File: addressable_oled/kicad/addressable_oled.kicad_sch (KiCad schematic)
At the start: 1 part

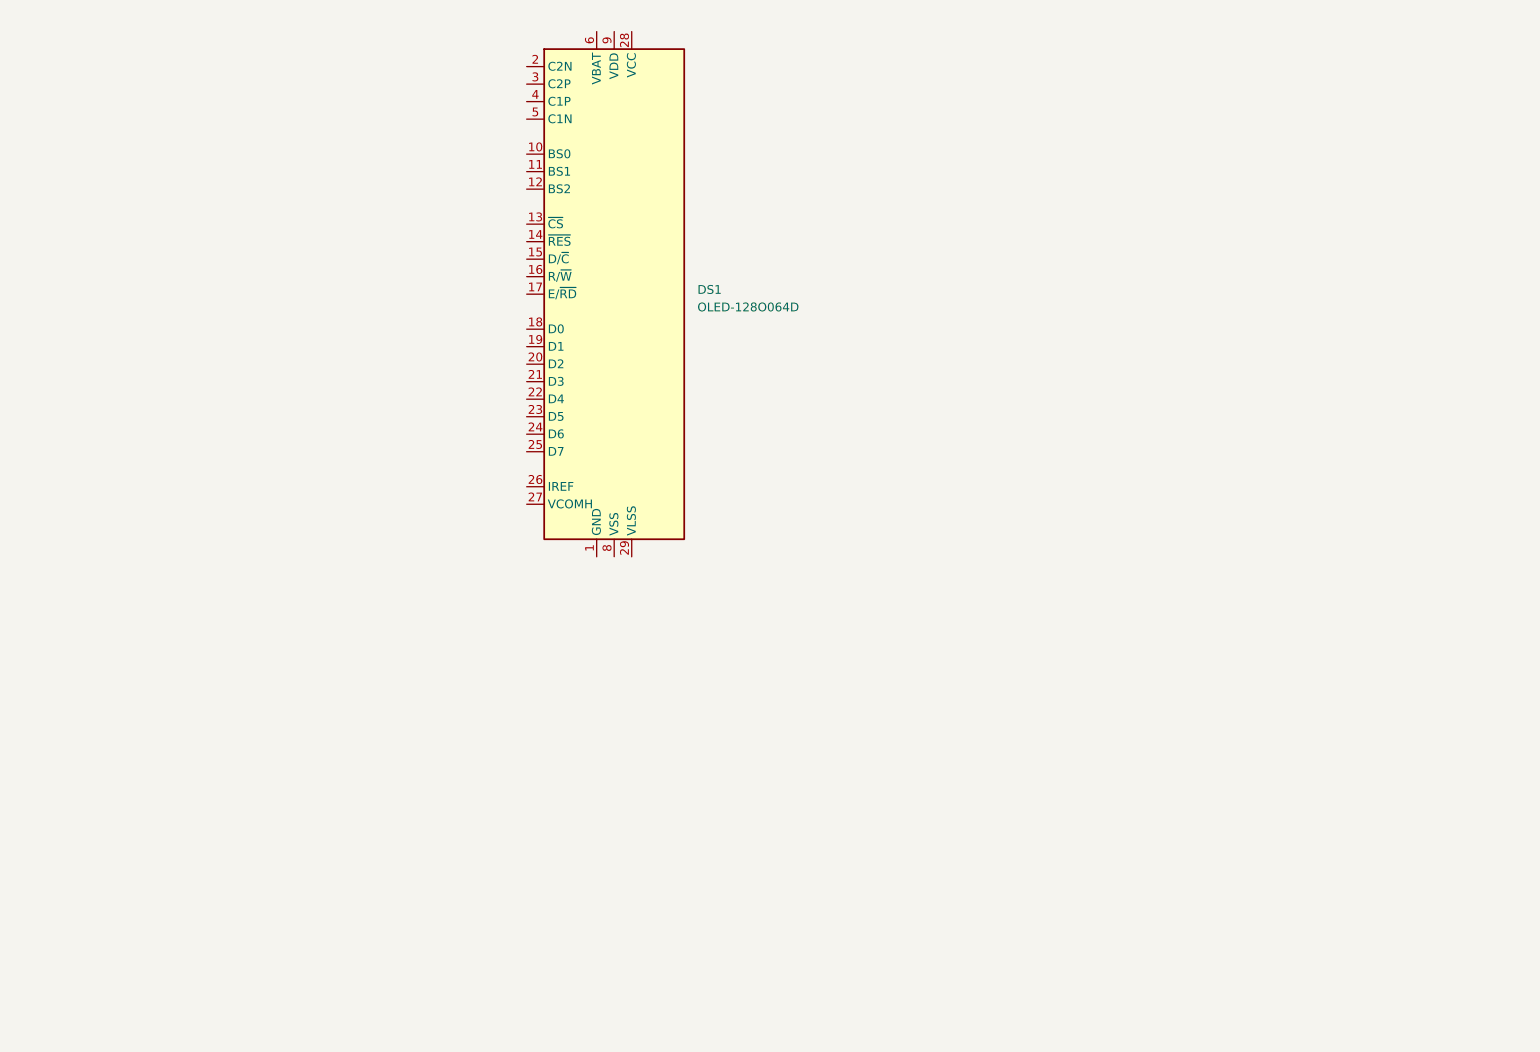
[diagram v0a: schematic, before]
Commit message: Work in progress. Added symbols and footprints.
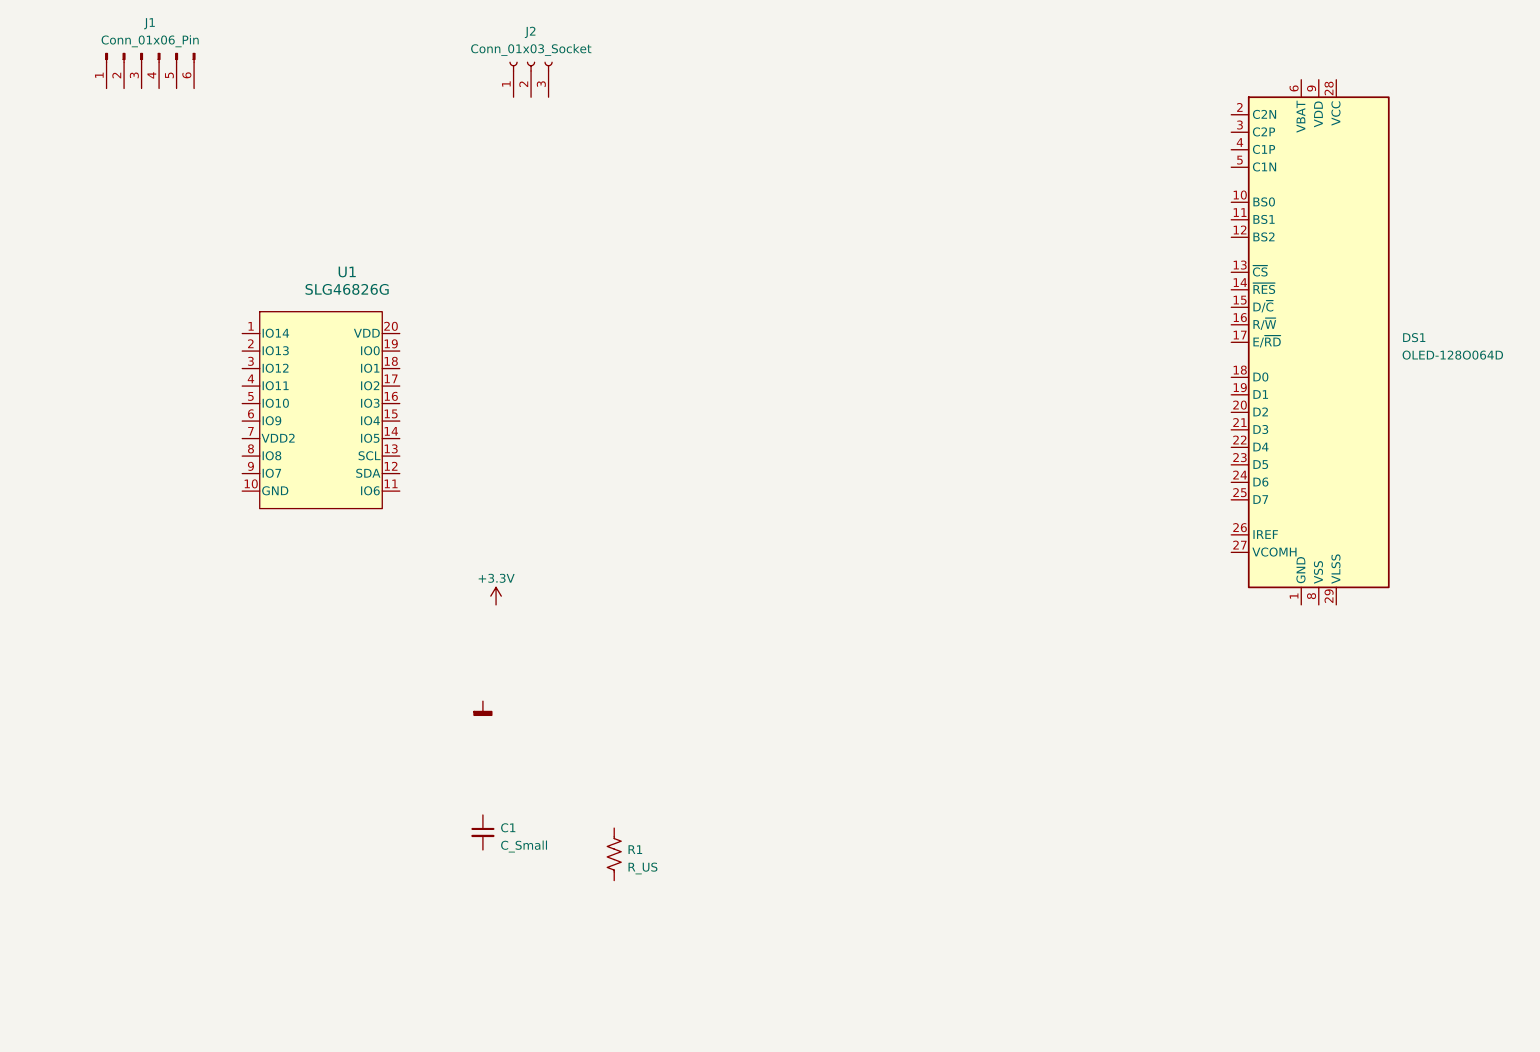
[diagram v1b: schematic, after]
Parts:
- added C1: C_Small, symbol Device:C_Small
- added J1: Conn_01x06_Pin, symbol Connector:Conn_01x06_Pin
- added J2: Conn_01x03_Socket, symbol Connector:Conn_01x03_Socket
- added R1: R_US, symbol Device:R_US
- added U1: SLG46826G, addressable_oled:TSSOP20_MO-220_WECE_REN, symbol addressable_oled:SLG46826G
- DS1: footprint Display:OLED-128O064D -> addressable_oled:OLED-128O064D; symbol Display_Graphic:OLED-128O064D -> addressable_oled:OLED-128O064D
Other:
- moved on the sheet: DS1
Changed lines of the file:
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@@
 (kicad_sch (version 20230121) (generator eeschema)
   (paper "A4")
-  (symbol (lib_id "Display_Graphic:OLED-128O064D") (at 123.825 85.09 0) (unit 1)
-    (in_bom yes) (on_board yes) (dnp no) (fields_autoplaced)
-    (property "Reference" "DS1" (at 135.89 84.455 0)
-      (effects (font (size 1.27 1.27)) (justify left))
-    )
-    (property "Value" "OLED-128O064D" (at 135.89 86.995 0)
-      (effects (font (size 1.27 1.27)) (justify left))
-    )
-    (property "Footprint" "Display:OLED-128O064D" (at 123.825 85.09 0)
-      (effects (font (size 1.27 1.27)) hide)
-    )
-    (property "Datasheet" "https://www.vishay.com/docs/37902/oled128o064dbpp3n00000.pdf" (at 123.825 64.77 0)
+  (symbol (lib_id "Connector:Conn_01x06_Pin") (at 55.245 50.165 90) (mirror x) (unit 1)
+    (in_bom yes) (on_board yes) (dnp no)
+    (property "Reference" "J1" (at 56.515 45.72 90)
+      (effects (font (size 1.27 1.27)))
+    )
+    (property "Value" "Conn_01x06_Pin" (at 56.515 48.26 90)
+      (effects (font (size 1.27 1.27)))
+    )
+    (property "Footprint" "" (at 55.245 50.165 0)
+      (effects (font (size 1.27 1.27)) hide)
+    )
+    (property "Datasheet" "~" (at 55.245 50.165 0)
+      (effects (font (size 1.27 1.27)) hide)
+    )
+    (pin "1")
+    (pin "2")
+    (pin "3")
+    (pin "4")
+    (pin "5")
+    (pin "6")
+    (instances
+      (project "addressable_oled"
+        (path "/7b608d4d-4c17-4227-91f9-c343a36b0392"
+          (reference "J1") (unit 1)
+        )
+      )
+    )
+  )
+  (symbol (lib_id "Device:C_Small") (at 104.775 163.195 0) (unit 1)
+    (in_bom yes) (on_board yes) (dnp no) (fields_autoplaced)
+    (property "Reference" "C1" (at 107.315 162.5663 0)
+      (effects (font (size 1.27 1.27)) (justify left))
+    )
+    (property "Value" "C_Small" (at 107.315 165.1063 0)
+      (effects (font (size 1.27 1.27)) (justify left))
+    )
+    (property "Footprint" "" (at 104.775 163.195 0)
+      (effects (font (size 1.27 1.27)) hide)
+    )
+    (property "Datasheet" "~" (at 104.775 163.195 0)
+      (effects (font (size 1.27 1.27)) hide)
+    )
+    (pin "1")
+    (pin "2")
+    (instances
+      (project "addressable_oled"
+        (path "/7b608d4d-4c17-4227-91f9-c343a36b0392"
+          (reference "C1") (unit 1)
+        )
+      )
+    )
+  )
+  (symbol (lib_id "Device:R_US") (at 123.825 166.37 0) (unit 1)
+    (in_bom yes) (on_board yes) (dnp no) (fields_autoplaced)
+    (property "Reference" "R1" (at 125.73 165.735 0)
+      (effects (font (size 1.27 1.27)) (justify left))
+    )
+    (property "Value" "R_US" (at 125.73 168.275 0)
+      (effects (font (size 1.27 1.27)) (justify left))
+    )
+    (property "Footprint" "" (at 124.841 166.624 90)
+      (effects (font (size 1.27 1.27)) hide)
+    )
+    (property "Datasheet" "~" (at 123.825 166.37 0)
+      (effects (font (size 1.27 1.27)) hide)
+    )
+    (pin "1")
+    (pin "2")
+    (instances
+      (project "addressable_oled"
+        (path "/7b608d4d-4c17-4227-91f9-c343a36b0392"
+          (reference "R1") (unit 1)
+        )
+      )
+    )
+  )
+  (symbol (lib_id "addressable_oled:OLED-128O064D") (at 226.06 92.075 0) (unit 1)
+    (in_bom yes) (on_board yes) (dnp no) (fields_autoplaced)
+    (property "Reference" "DS1" (at 238.125 91.44 0)
+      (effects (font (size 1.27 1.27)) (justify left))
+    )
+    (property "Value" "OLED-128O064D" (at 238.125 93.98 0)
+      (effects (font (size 1.27 1.27)) (justify left))
+    )
+    (property "Footprint" "addressable_oled:OLED-128O064D" (at 226.06 92.075 0)
+      (effects (font (size 1.27 1.27)) hide)
+    )
+    (property "Datasheet" "https://www.vishay.com/docs/37902/oled128o064dbpp3n00000.pdf" (at 226.06 71.755 0)
       (effects (font (size 1.27 1.27)) hide)
     )
@@
         )
       )
+    )
+  )
+  (symbol (lib_id "addressable_oled:GND") (at 104.775 144.145 0) (unit 1)
+    (in_bom yes) (on_board yes) (dnp no) (fields_autoplaced)
+    (property "Reference" "#PWR02" (at 104.775 150.495 0)
+      (effects (font (size 1.27 1.27)) hide)
+    )
+    (property "Value" "GND" (at 104.775 149.225 0)
+      (effects (font (size 1.27 1.27)) hide)
+    )
+    (property "Footprint" "" (at 104.775 144.145 0)
+      (effects (font (size 1.27 1.27)) hide)
+    )
+    (property "Datasheet" "" (at 104.775 144.145 0)
+      (effects (font (size 1.27 1.27)) hide)
+    )
+    (pin "1")
+    (instances
+      (project "addressable_oled"
+        (path "/7b608d4d-4c17-4227-91f9-c343a36b0392"
+          (reference "#PWR02") (unit 1)
+        )
+      )
+    )
+  )
+  (symbol (lib_id "Connector:Conn_01x03_Socket") (at 111.76 51.435 90) (unit 1)
+    (in_bom yes) (on_board yes) (dnp no) (fields_autoplaced)
+    (property "Reference" "J2" (at 111.76 46.99 90)
+      (effects (font (size 1.27 1.27)))
+    )
+    (property "Value" "Conn_01x03_Socket" (at 111.76 49.53 90)
+      (effects (font (size 1.27 1.27)))
+    )
+    (property "Footprint" "" (at 111.76 51.435 0)
+      (effects (font (size 1.27 1.27)) hide)
+    )
+    (property "Datasheet" "~" (at 111.76 51.435 0)
+      (effects (font (size 1.27 1.27)) hide)
+    )
+    (pin "1")
+    (pin "2")
+    (pin "3")
+    (instances
+      (project "addressable_oled"
+        (path "/7b608d4d-4c17-4227-91f9-c343a36b0392"
+          (reference "J2") (unit 1)
+        )
+      )
+    )
+  )
+  (symbol (lib_id "addressable_oled:SLG46826G") (at 64.77 90.805 0) (unit 1)
+    (in_bom yes) (on_board yes) (dnp no) (fields_autoplaced)
+    (property "Reference" "U1" (at 85.09 81.915 0)
+      (effects (font (size 1.524 1.524)))
+    )
+    (property "Value" "SLG46826G" (at 85.09 84.455 0)
+      (effects (font (size 1.524 1.524)))
+    )
+    (property "Footprint" "addressable_oled:TSSOP20_MO-220_WECE_REN" (at 64.77 90.805 0)
+      (effects (font (size 1.27 1.27) italic) hide)
+    )
+    (property "Datasheet" "SLG46826G" (at 64.77 90.805 0)
+      (effects (font (size 1.27 1.27) italic) hide)
+    )
+    (pin "1")
+    (pin "10")
+    (pin "11")
+    (pin "12")
+    (pin "13")
+    (pin "14")
+    (pin "15")
+    (pin "16")
+    (pin "17")
+    (pin "18")
+    (pin "19")
+    (pin "2")
+    (pin "20")
+    (pin "3")
+    (pin "4")
+    (pin "5")
+    (pin "6")
+    (pin "7")
+    (pin "8")
+    (pin "9")
+    (instances
+      (project "addressable_oled"
+        (path "/7b608d4d-4c17-4227-91f9-c343a36b0392"
+          (reference "U1") (unit 1)
+        )
+      )
+    )
+  )
+  (symbol (lib_id "power:+3.3V") (at 106.68 130.175 0) (unit 1)
+    (in_bom yes) (on_board yes) (dnp no) (fields_autoplaced)
+    (property "Reference" "#PWR01" (at 106.68 133.985 0)
+      (effects (font (size 1.27 1.27)) hide)
+    )
+    (property "Value" "+3.3V" (at 106.68 126.365 0)
+      (effects (font (size 1.27 1.27)))
+    )
+    (property "Footprint" "" (at 106.68 130.175 0)
+      (effects (font (size 1.27 1.27)) hide)
+    )
+    (property "Datasheet" "" (at 106.68 130.175 0)
+      (effects (font (size 1.27 1.27)) hide)
+    )
+    (pin "1")
+    (instances
+      (project "addressable_oled"
+        (path "/7b608d4d-4c17-4227-91f9-c343a36b0392"
+          (reference "#PWR01") (unit 1)
+        )
+      )

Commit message: Work in progress. First pass of the schematic.
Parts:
- added C2, C3, C4, C5, C6, C7, C8: C_Small, symbol Device:C_Small
- added JP1, JP2, JP?: Jumper_2_Open, symbol addressable_oled:Jumper_2_Open
- added R5, R6: R_US, symbol Device:R_US
- J1: value Conn_01x06_Pin -> Conn_01x05_Pin; symbol Connector:Conn_01x06_Pin -> Connector:Conn_01x05_Pin
- renumbered DS1 to DS?
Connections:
- net GND: now also C1.1, DS?.1 (GND), DS?.10 (BS0), DS?.11 (BS1), DS?.12 (BS2), DS?.16 (R/~{W}), DS?.17 (E/~{RD}), DS?.20 (D2), DS?.21 (D3), DS?.22 (D4), DS?.23 (D5), DS?.24 (D6), DS?.25 (D7), DS?.29 (VLSS), DS?.30 (GND), DS?.8 (VSS), J1.1 (Pin_1), J2.1 (Pin_1), R1.2, U1.10 (GND), C2.2, C3.1, C4.1, C5.2, C8.1
- net 3V3: now reaches J1.2 (Pin_2)
- net 3V3: now also C1.2, DS?.6 (VBAT), DS?.9 (VDD), U1.20 (VDD), U1.7 (VDD2), C2.1, C3.2, C4.2, JP1.2, JP2.2, JP?.2, R5.1, R6.1
- net CS: now reaches J1.3 (Pin_3)
- net CS: now also U1.1 (IO14)
- net CLK: now reaches J1.4 (Pin_4)
- net CLK: now also U1.2 (IO13)
- net MOSI: now reaches J1.5 (Pin_5)
- net MOSI: now also U1.3 (IO12)
- net at R1.1: now also DS?.26 (IREF)
- net OLED_CS: now reaches DS?.13 (~{CS})
- net OLED_CS: now also U1.4 (IO11)
- net OLED_RST: now reaches DS?.14 (~{RES})
- net OLED_RST: now also U1.8 (IO8)
- net OLED_DC: now reaches DS?.15 (D/~{C})
- net OLED_DC: now also U1.9 (IO7)
- net OLED_CLK: now reaches DS?.18 (D0)
- net OLED_CLK: now also U1.5 (IO10)
- net OLED_MOSI: now reaches DS?.19 (D1)
- net OLED_MOSI: now also U1.6 (IO9)
- net at DS?.2 (C2N): now also C7.1
- net at DS?.27 (VCOMH): now also C8.2
- net at DS?.28 (VCC): now also C5.1
- net at DS?.3 (C2P): now also C7.2
- net at DS?.4 (C1P): now also C6.1
- net at DS?.5 (C1N): now also C6.2
- net I2C_DAT: now reaches J2.2 (Pin_2)
- net I2C_DAT: now also U1.12 (SDA), R5.2
- net I2C_CLK: now reaches J2.3 (Pin_3)
- net I2C_CLK: now also U1.13 (SCL), R6.2
- net at U1.15 (IO4): now also JP?.1~ (A)
- net at U1.16 (IO3): now also JP1.1~ (A)
- net at U1.17 (IO2): now also JP2.1~ (A)
- no-connect marks 0 -> 4
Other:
- note added: "TODO: Revisit ALL OLED pins"
- note added: "TODO: Revisit GreenPAK pins"
- note added: "TODO: Revisit pin 20"
- moved on the sheet: C1, J2, U1

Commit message: More progress with the schematic and layout.
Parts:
- added C9: 2u2, Capacitor_SMD:C_0603_1608Metric, symbol Device:C_Small
- C1: renamed from C2; value C_Small -> 100n; footprint (none) -> Capacitor_SMD:C_0603_1608Metric
- C2: renamed from C3; value C_Small -> 100n; footprint (none) -> Capacitor_SMD:C_0603_1608Metric
- C3: renamed from C8; value C_Small -> 2u2; footprint (none) -> Capacitor_SMD:C_0603_1608Metric
- C4: renamed from C7; value C_Small -> 1u; footprint (none) -> Capacitor_SMD:C_0603_1608Metric
- C5: renamed from C6; value C_Small -> 1u; footprint (none) -> Capacitor_SMD:C_0603_1608Metric
- C6: renamed from C4; value C_Small -> 100n; footprint (none) -> Capacitor_SMD:C_0603_1608Metric
- C7: renamed from C1; value C_Small -> 100n; footprint (none) -> Capacitor_SMD:C_0603_1608Metric
- C8: renamed from C5; value C_Small -> 100n; footprint (none) -> Capacitor_SMD:C_0603_1608Metric
- J1: footprint (none) -> Connector_PinHeader_2.54mm:PinHeader_1x05_P2.54mm_Vertical
- J2: footprint (none) -> Connector_PinHeader_2.54mm:PinHeader_1x03_P2.54mm_Vertical
- JP1: renamed from JP2; footprint (none) -> Jumper:SolderJumper-2_P1.3mm_Open_Pad1.0x1.5mm
- JP2: renamed from JP1; footprint (none) -> Jumper:SolderJumper-2_P1.3mm_Open_Pad1.0x1.5mm
- JP4: renamed from JP?; footprint (none) -> Jumper:SolderJumper-2_P1.3mm_Open_Pad1.0x1.5mm
- R1: renamed from R5; value R_US -> 5K; footprint (none) -> Resistor_SMD:R_0603_1608Metric
- R2: renamed from R6; value R_US -> 5K; footprint (none) -> Resistor_SMD:R_0603_1608Metric
- R3: renamed from R1; value R_US -> 910K; footprint (none) -> Resistor_SMD:R_0603_1608Metric
- gave numbers to parts that had none: 1
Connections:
- net GND: now also C9.2; no longer U2.20 (D2)
- net at U1.16 (IO3): now also JP2.1; no longer JP2.1~ (A)
- net at C8.1, U2.28 (VCC): now also C9.1
- net at U1.17 (IO2): now also JP1.1; no longer JP1.1~ (A)
- net at U1.15 (IO4): now also JP4.1; no longer JP4.1~ (A)
- net 3V3 renamed VDD
- no-connect marks 4 -> 6
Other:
- moved on the sheet: C2, C8, J1
